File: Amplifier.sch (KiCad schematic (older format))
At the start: 28 parts, among them U1 TDA7283

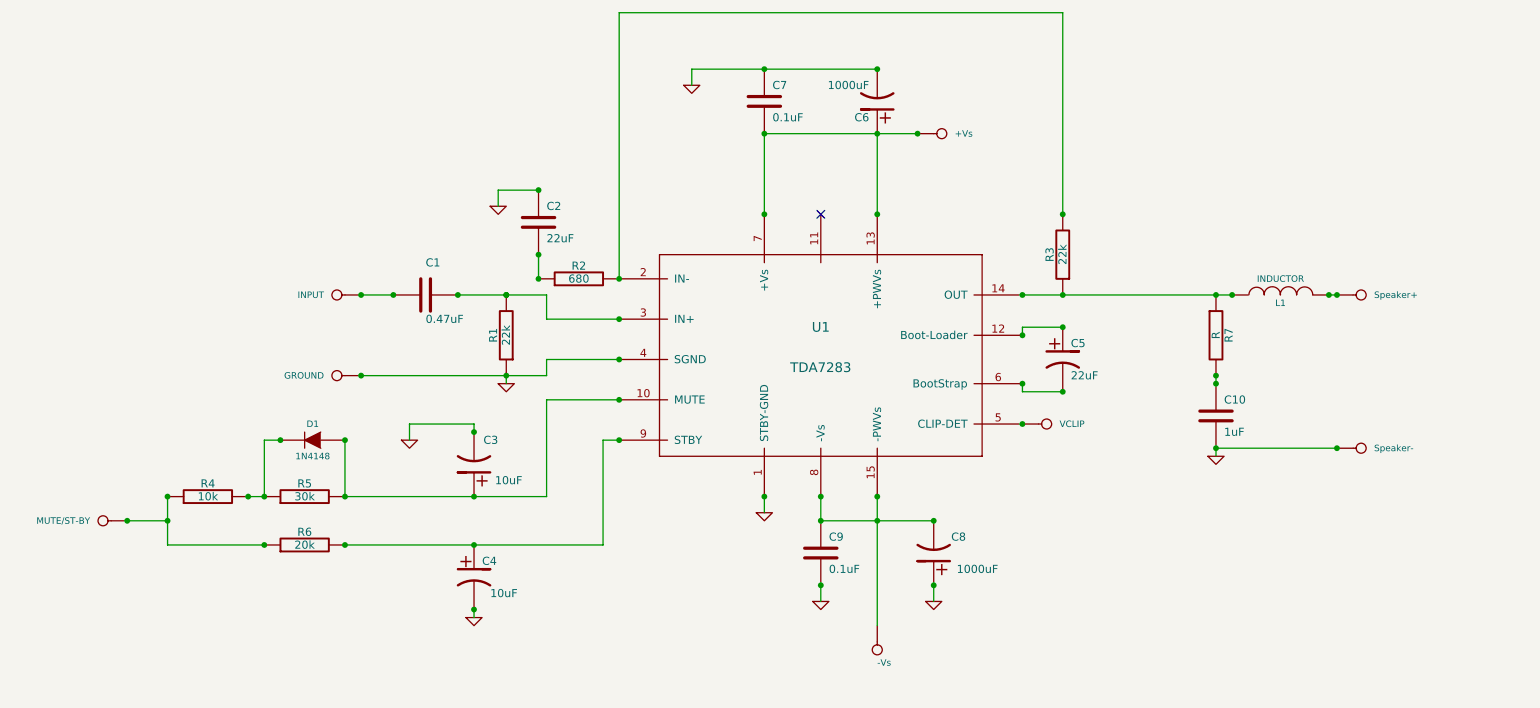
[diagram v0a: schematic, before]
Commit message: Made the changes specified at http://forum.diyefi.org/viewtopic.php?p=32437#p32437 Which changed C2 and C5 to 100uF, triple decouple capacitors for both power supply rails, changed input C1 from 0.47uF to 3x 1uF capacitors in parallel and changed diode D1 to 1N4007.
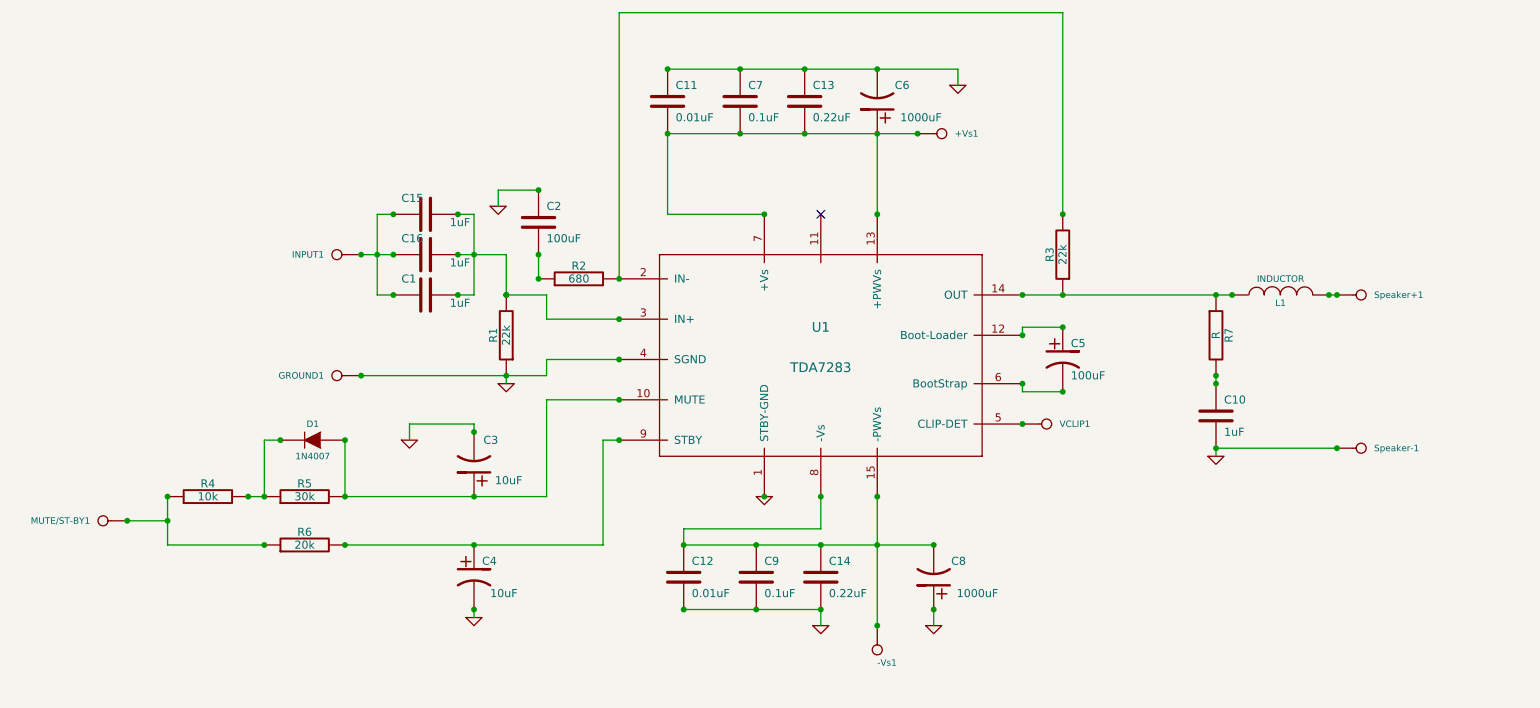
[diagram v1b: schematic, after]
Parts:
- added C11, C12: 0.01uF, symbol C
- added C13, C14: 0.22uF, symbol C
- added C15, C16: 1uF, symbol C
- C1: value 0.47uF -> 1uF
- C2, C5: value 22uF -> 100uF
- D1: value 1N4148 -> 1N4007
- renumbered +Vs to +Vs1, -Vs to -Vs1, GROUND to GROUND1, INPUT to INPUT1, MUTE/ST-BY to MUTE/ST-BY1, Speaker+ to Speaker+1, Speaker- to Speaker-1, VCLIP to VCLIP1
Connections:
- net GND: now also C11.1, C12.2, C13.1, C14.2
- net at +Vs1.1, C6.1 (+), C7.2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: now also C11.2, C13.2
- net at -Vs1.1, C8.2 (-), C9.1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: now also C12.1, C14.1
- net at C1.1, R1.2, U1.3 (IN+): now also C15.1, C16.1
- net at C1.2, INPUT1.1: now also C15.2, C16.2
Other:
- moved on the sheet: C7, C8, C9, INPUT1

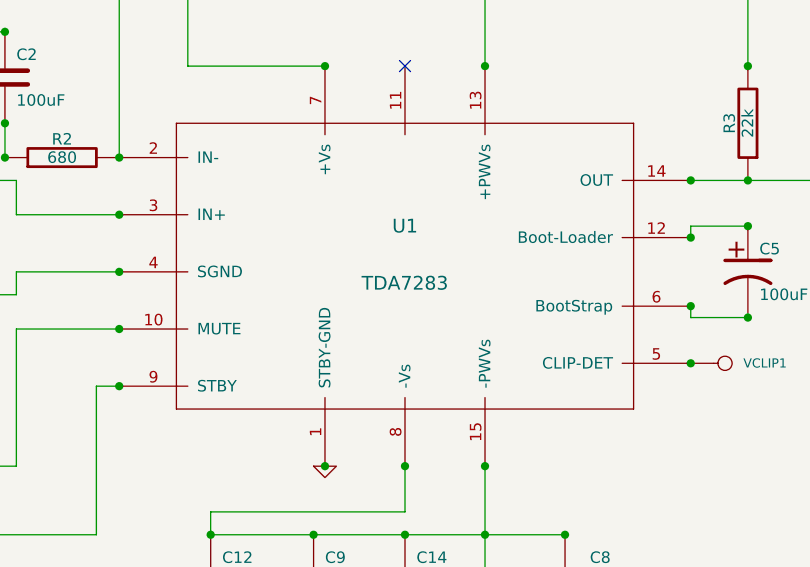
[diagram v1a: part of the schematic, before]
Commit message: Changed IC part number from TDA7283 to TDA7293.  Thanks Fred Cooke for catching that error!
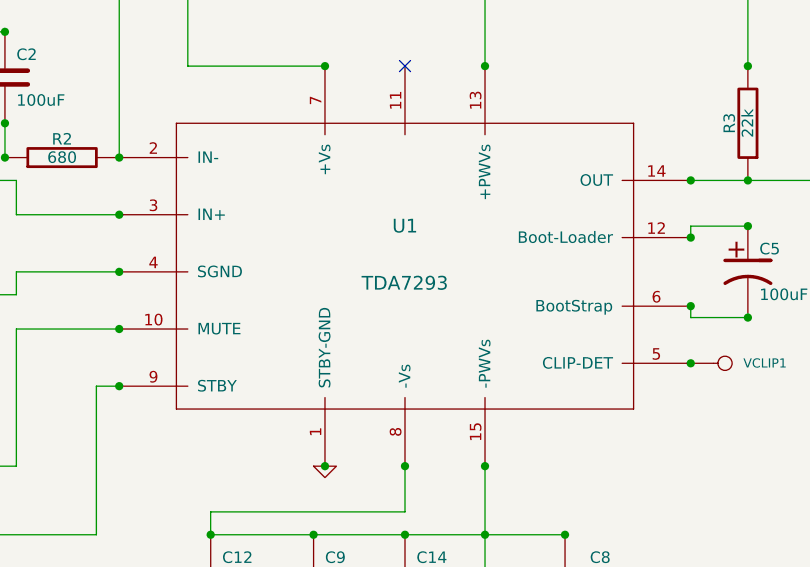
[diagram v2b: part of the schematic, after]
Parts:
- U1: value TDA7283 -> TDA7293
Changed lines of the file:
@@
-EESchema Schematic File Version 2  date Mon 04 Feb 2013 02:15:49 PM EST
+EESchema Schematic File Version 2  date Sun 02 Jun 2013 12:15:59 AM EDT
 LIBS:power
 LIBS:device
@@
 Sheet 1 1
 Title "ST Microelectronics TDA7293 Amplifier"
-Date "4 feb 2013"
+Date "2 jun 2013"
 Rev "0.1-alpha"
 Comp "Drawn by: Andy Goss"
@@
 $EndComp
 $Comp
-L GND #PWR9
+L GND #PWR01
 U 1 1 510DAD2C
 P 8200 4400
-F 0 "#PWR9" H 8200 4400 30  0001 C CNN
+F 0 "#PWR01" H 8200 4400 30  0001 C CNN
 F 1 "GND" H 8200 4330 30  0001 C CNN
 	1    8200 4400
@@
 $EndComp
 $Comp
-L GND #PWR2
+L GND #PWR02
 U 1 1 510DABAE
 P 3600 5400
-F 0 "#PWR2" H 3600 5400 30  0001 C CNN
+F 0 "#PWR02" H 3600 5400 30  0001 C CNN
 F 1 "GND" H 3600 5330 30  0001 C CNN
 	1    3600 5400
@@
 $EndComp
 $Comp
-L GND #PWR1
+L GND #PWR03
 U 1 1 510DABA5
 P 3200 4300
-F 0 "#PWR1" H 3200 4300 30  0001 C CNN
+F 0 "#PWR03" H 3200 4300 30  0001 C CNN
 F 1 "GND" H 3200 4230 30  0001 C CNN
 	1    3200 4300
@@
 $EndComp
 $Comp
-L GND #PWR5
+L GND #PWR04
 U 1 1 510DAAE7
 P 5400 4650
-F 0 "#PWR5" H 5400 4650 30  0001 C CNN
+F 0 "#PWR04" H 5400 4650 30  0001 C CNN
 F 1 "GND" H 5400 4580 30  0001 C CNN
 	1    5400 4650
@@
 $EndComp
 $Comp
-L GND #PWR6
+L GND #PWR05
 U 1 1 510DAAB0
 P 5750 5450
-F 0 "#PWR6" H 5750 5450 30  0001 C CNN
+F 0 "#PWR05" H 5750 5450 30  0001 C CNN
 F 1 "GND" H 5750 5380 30  0001 C CNN
 	1    5750 5450
@@
 $EndComp
 $Comp
-L GND #PWR7
+L GND #PWR06
 U 1 1 510DAA8C
 P 6450 5450
-F 0 "#PWR7" H 6450 5450 30  0001 C CNN
+F 0 "#PWR06" H 6450 5450 30  0001 C CNN
 F 1 "GND" H 6450 5380 30  0001 C CNN
 	1    6450 5450
@@
 $EndComp
 $Comp
-L GND #PWR4
+L GND #PWR07
 U 1 1 510DAA17
 P 3800 3950
-F 0 "#PWR4" H 3800 3950 30  0001 C CNN
+F 0 "#PWR07" H 3800 3950 30  0001 C CNN
 F 1 "GND" H 3800 3880 30  0001 C CNN
 	1    3800 3950
@@
 $EndComp
 $Comp
-L GND #PWR3
+L GND #PWR08
 U 1 1 510DA8B8
 P 3750 2850
-F 0 "#PWR3" H 3750 2850 30  0001 C CNN
+F 0 "#PWR08" H 3750 2850 30  0001 C CNN
 F 1 "GND" H 3750 2780 30  0001 C CNN
 	1    3750 2850
@@
 $EndComp
 $Comp
-L GND #PWR8
+L GND #PWR09
 U 1 1 510DA565
 P 6600 2100
-F 0 "#PWR8" H 6600 2100 30  0001 C CNN
+F 0 "#PWR09" H 6600 2100 30  0001 C CNN
 F 1 "GND" H 6600 2030 30  0001 C CNN
 	1    6600 2100
@@
 P 5750 3800
 F 0 "U1" H 5750 4000 60  0000 C CNN
-F 1 "TDA7283" H 5750 3750 60  0000 C CNN
+F 1 "TDA7293" H 5750 3750 60  0000 C CNN
 	1    5750 3800
 	1    0    0    -1

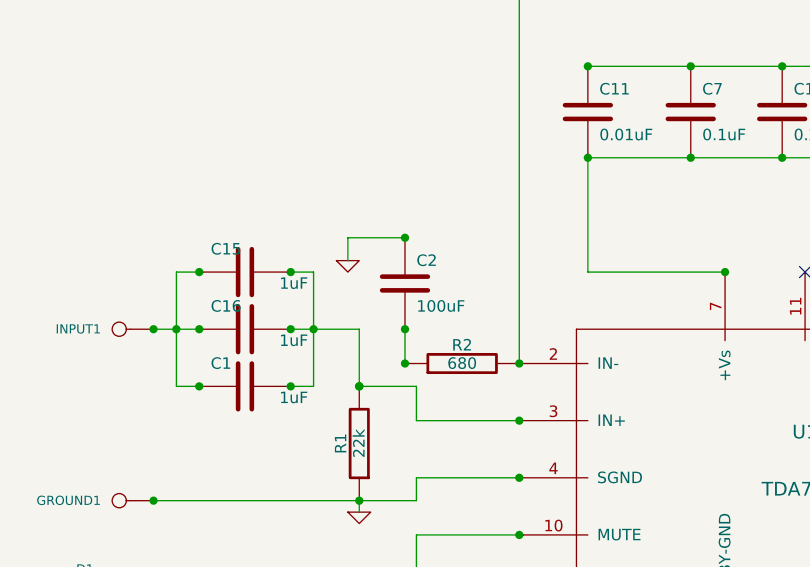
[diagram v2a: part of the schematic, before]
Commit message: Initial routing of the circuit board.
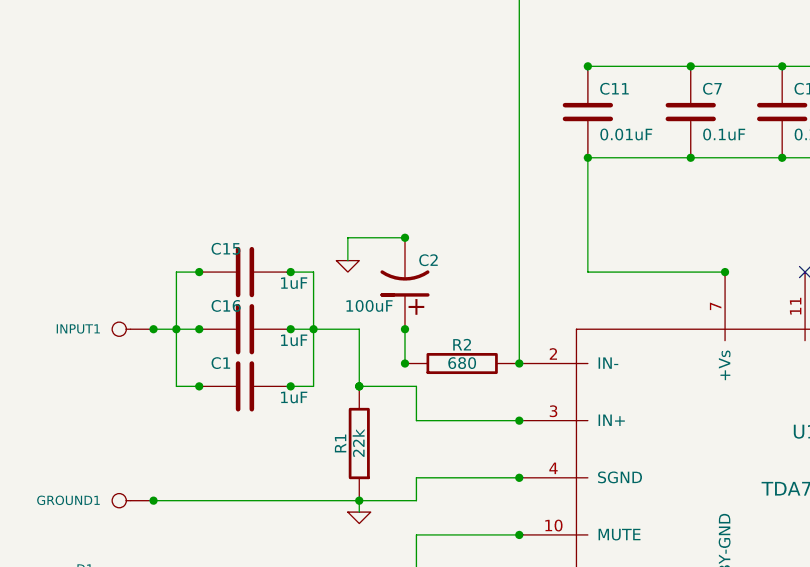
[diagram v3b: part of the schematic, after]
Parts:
- removed C2: 100uF, symbol C
- added C2: 100uF, symbol CP1
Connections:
- net GND: now also C2.2 (-)
- net at R2.1: now also C2.1 (+)
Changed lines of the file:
@@
-EESchema Schematic File Version 2  date Sun 02 Jun 2013 12:15:59 AM EDT
+EESchema Schematic File Version 2  date Sun 02 Jun 2013 12:35:52 PM EDT
 LIBS:power
 LIBS:device
@@
 Comment4 ""
 $EndDescr
+$Comp
+L CP1 C2
+U 1 1 51AB7445
+P 4000 2950
+F 0 "C2" H 3850 2850 50  0000 L CNN
+F 1 "100uF" H 4050 3050 50  0000 L CNN
+	1    4000 2950
+	-1   0    0    1
+$EndComp
 Connection ~ 4800 2400
 Connection ~ 4800 2000
@@
 	1    0    0    -1
 $EndComp
-$Comp
-L C C2
-U 1 1 510DA895
-P 4000 2950
-F 0 "C2" H 4050 3050 50  0000 L CNN
-F 1 "100uF" H 4050 2850 50  0000 L CNN
-	1    4000 2950
-	1    0    0    -1
-$EndComp

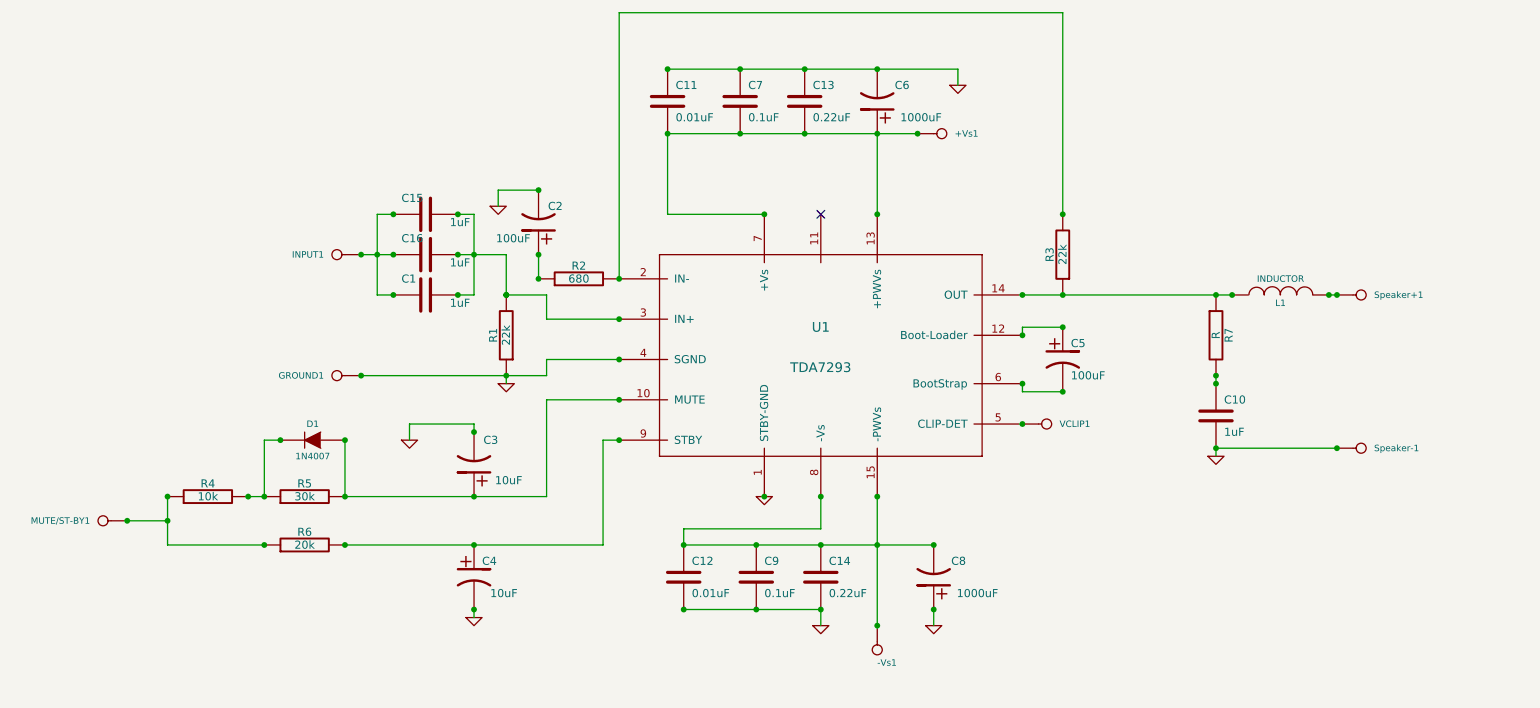
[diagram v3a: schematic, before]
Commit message: Made R7 larger, made C1, C15, C16 larger, moved triple decoupling capacitors closer to U1.
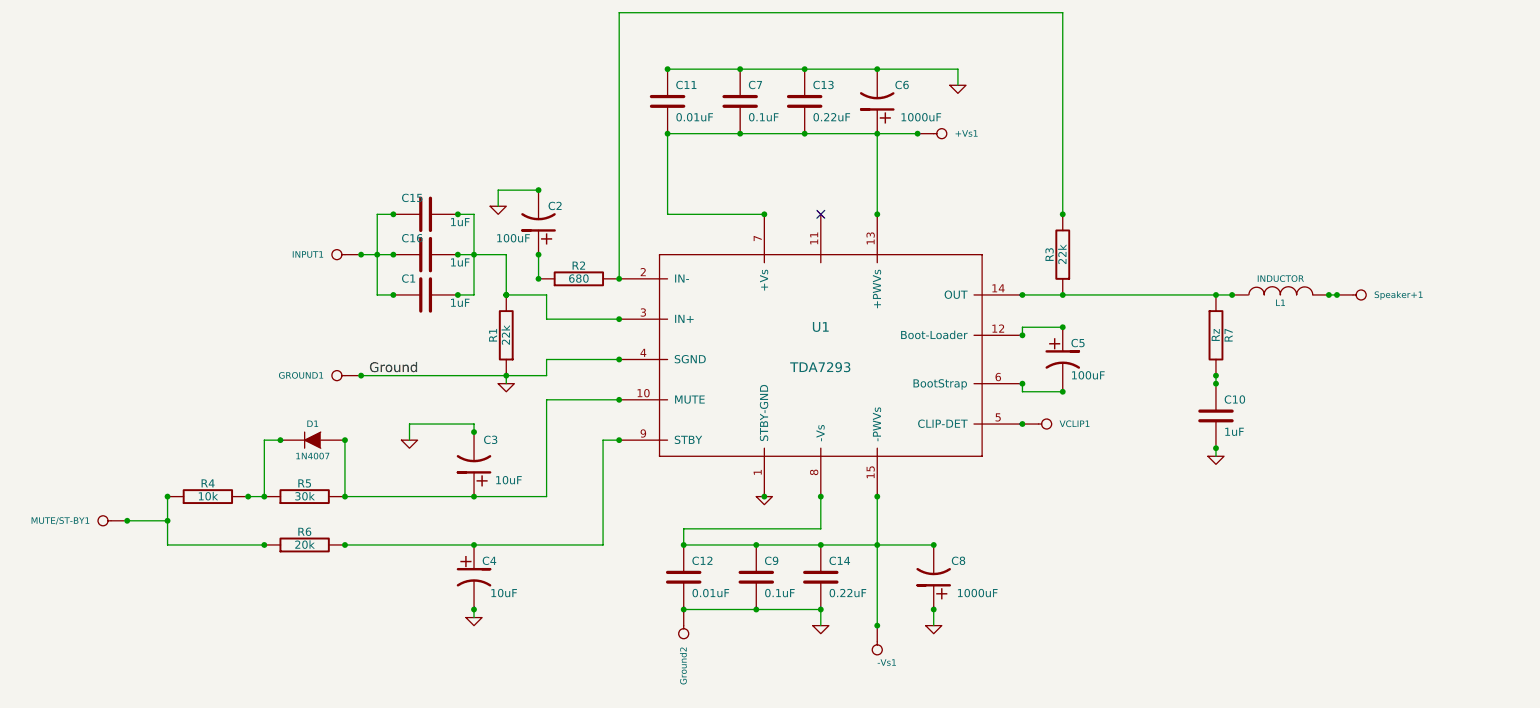
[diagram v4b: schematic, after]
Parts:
- R7: value R -> Rz
- renumbered Speaker-1 to Ground2
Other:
- moved on the sheet: Ground2
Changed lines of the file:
@@
-EESchema Schematic File Version 2  date Sun 02 Jun 2013 12:35:52 PM EDT
+EESchema Schematic File Version 2  date Sun 02 Jun 2013 07:10:17 PM EDT
 LIBS:power
 LIBS:device
@@
 Comment4 ""
 $EndDescr
+Text Label 2950 3900 0    60   ~ 0
+Ground
 $Comp
 L CP1 C2
@@
 Connection ~ 3600 5350
 Wire Wire Line
-	8200 4350 8950 4350
-Wire Wire Line
 	8200 3900 8200 3950
 Wire Wire Line
@@
 Connection ~ 8200 3950
 Connection ~ 8200 4350
-Connection ~ 8950 4350
 Wire Wire Line
 	6600 2000 6600 2100
@@
 $EndComp
 $Comp
-L CONN_1 Speaker-1
+L CONN_1 Ground2
 U 1 1 510DAD41
-P 9100 4350
-F 0 "Speaker-1" H 9180 4350 40  0000 L CNN
-F 1 "CONN_1" H 9100 4405 30  0001 C CNN
-	1    9100 4350
-	1    0    0    -1
+P 4900 5500
+F 0 "Ground2" H 4980 5500 40  0000 L CNN
+F 1 "CONN_1" H 4900 5555 30  0001 C CNN
+	1    4900 5500
+	0    1    1    0
 $EndComp
 $Comp
@@
 P 8200 3650
 F 0 "R7" V 8280 3650 50  0000 C CNN
-F 1 "R" V 8200 3650 50  0000 C CNN
+F 1 "Rz" V 8200 3650 50  0000 C CNN
 	1    8200 3650
 	1    0    0    -1

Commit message: Made mounting holes 2.2mm diameter with 3.5mm pads that are not connected to the ground plane.
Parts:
- added H1, H2, H3, H4: CONN_1, symbol CONN_1
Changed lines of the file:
@@
-EESchema Schematic File Version 2  date Sun 02 Jun 2013 07:10:17 PM EDT
+EESchema Schematic File Version 2  date Sun 02 Jun 2013 07:50:12 PM EDT
 LIBS:power
 LIBS:device
@@
 Comment4 ""
 $EndDescr
+$Comp
+L CONN_1 H4
+U 1 1 51ABDA12
+P 9950 5800
+F 0 "H4" H 10030 5800 40  0000 L CNN
+F 1 "CONN_1" H 9950 5855 30  0001 C CNN
+	1    9950 5800
+	1    0    0    -1
+$EndComp
+$Comp
+L CONN_1 H3
+U 1 1 51ABDA0C
+P 9950 5600
+F 0 "H3" H 10030 5600 40  0000 L CNN
+F 1 "CONN_1" H 9950 5655 30  0001 C CNN
+	1    9950 5600
+	1    0    0    -1
+$EndComp
+$Comp
+L CONN_1 H2
+U 1 1 51ABDA06
+P 9950 5400
+F 0 "H2" H 10030 5400 40  0000 L CNN
+F 1 "CONN_1" H 9950 5455 30  0001 C CNN
+	1    9950 5400
+	1    0    0    -1
+$EndComp
+$Comp
+L CONN_1 H1
+U 1 1 51ABD9FC
+P 9950 5200
+F 0 "H1" H 10030 5200 40  0000 L CNN
+F 1 "CONN_1" H 9950 5255 30  0001 C CNN
+	1    9950 5200
+	1    0    0    -1
+$EndComp
 Text Label 2950 3900 0    60   ~ 0
 Ground
